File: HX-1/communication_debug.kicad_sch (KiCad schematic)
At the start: 28 parts, among them J1 USB_C_Receptacle_USB2.0_16P, U2 USBLC6-2SC6, U4 LSM6DS3

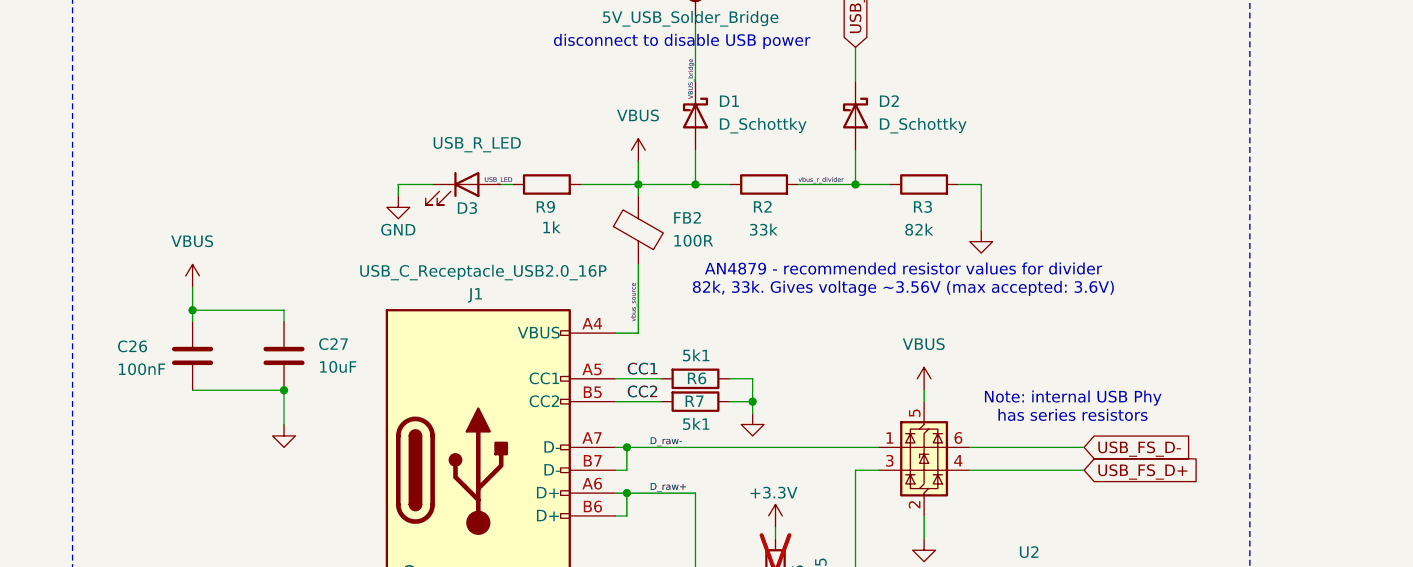
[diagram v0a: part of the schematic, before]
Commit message: change USB capacitors to be fueled from VBUS_raw
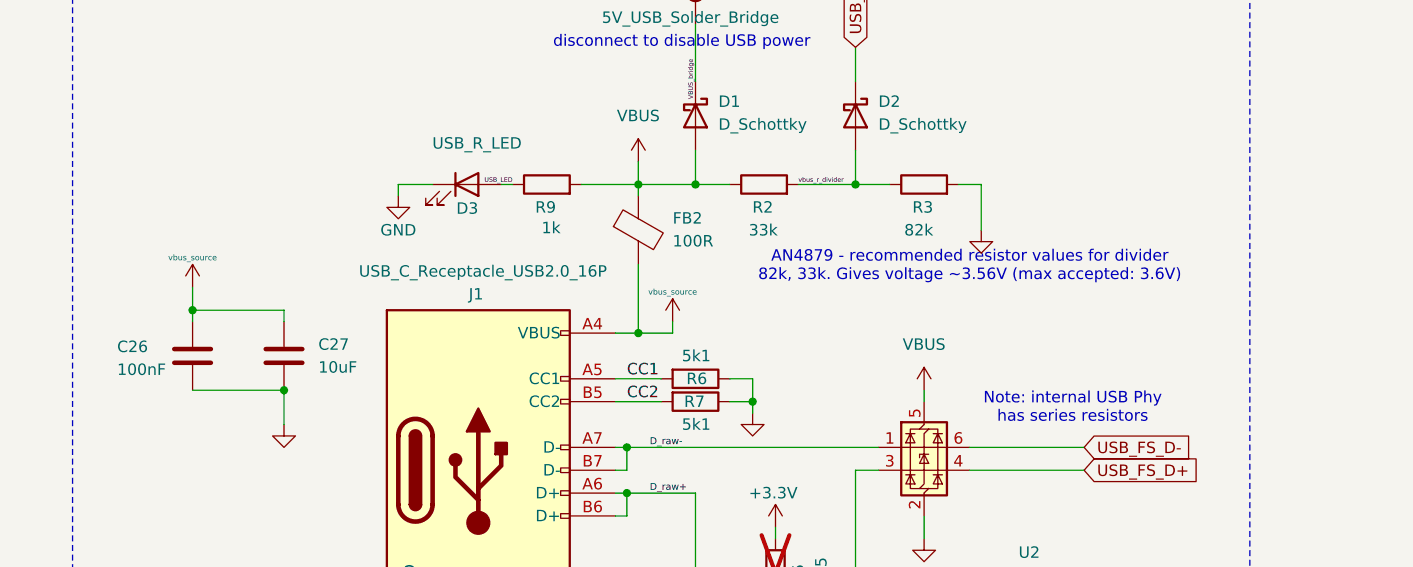
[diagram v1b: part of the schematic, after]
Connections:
- net VBUS: no longer C26.1, C27.1
- net vbus_source: now also C26.1, C27.1
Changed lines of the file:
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@@
 	)
 	(junction
+		(at 158.75 74.93)
+		(diameter 0)
+		(color 0 0 0 0)
+	)
+	(junction
 		(at 40.64 41.91)
 		(diameter 0)
@@
 	(wire
 		(pts
+			(xy 162.56 73.66) (xy 162.56 74.93)
+		)
+		(stroke
+			(width 0)
+			(type default)
+		)
+	)
+	(wire
+		(pts
 			(xy 57.15 59.69) (xy 57.15 60.96)
 		)
@@
 	(wire
 		(pts
+			(xy 158.75 74.93) (xy 162.56 74.93)
+		)
+		(stroke
+			(width 0)
+			(type default)
+		)
+	)
+	(wire
+		(pts
 			(xy 171.45 83.82) (xy 171.45 82.55)
 		)
@@
 	(text "AN4879 - recommended resistor values for divider\n82k, 33k. Gives voltage ~3.56V (max accepted: 3.6V)"
 		(exclude_from_sim no)
-		(at 188.214 69.088 0)
+		(at 195.58 67.564 0)
 		(effects
 			(font
@@
 		)
 	)
-	(label "vbus_source"
-		(at 158.75 73.66 90)
-		(effects
-			(font
-				(size 0.508 0.508)
-			)
-			(justify left bottom)
-		)
-	)
 	(label "VBUS_bridge"
 		(at 165.1 44.45 270)
@@
 	)
 	(symbol
-		(lib_id "power:+5V")
-		(at 109.22 69.85 0)
-		(unit 1)
-		(exclude_from_sim no)
-		(in_bom yes)
-		(on_board yes)
-		(dnp no)
-		(fields_autoplaced yes)
-		(property "Reference" "#PWR18"
-			(at 109.22 73.66 0)
-			(effects
-				(font
-					(size 1.27 1.27)
-				)
-				(hide yes)
-			)
-		)
-		(property "Value" "VBUS"
-			(at 109.22 64.77 0)
-			(effects
-				(font
-					(size 1.27 1.27)
-				)
-			)
-		)
-		(property "Footprint" ""
-			(at 109.22 69.85 0)
-			(effects
-				(font
-					(size 1.27 1.27)
-				)
-				(hide yes)
-			)
-		)
-		(property "Datasheet" ""
-			(at 109.22 69.85 0)
-			(effects
-				(font
-					(size 1.27 1.27)
-				)
-				(hide yes)
-			)
-		)
-		(property "Description" "Power symbol creates a global label with name \"+5V\""
-			(at 109.22 69.85 0)
-			(effects
-				(font
-					(size 1.27 1.27)
-				)
-				(hide yes)
-			)
-		)
-		(pin "1"
-		)
-		(instances
-			(project "HX-1"
-				(path "/a3219989-2bf1-44ea-9412-fab86edfb39b/f68304e7-586c-4481-9c91-394c7e636be5"
-					(reference "#PWR18")
-					(unit 1)
-				)
-			)
-		)
-	)
-	(symbol
 		(lib_id "power:GND")
 		(at 254.762 50.292 0)
@@
 	)
 	(symbol
+		(lib_id "power:+5V")
+		(at 109.22 69.85 0)
+		(unit 1)
+		(exclude_from_sim no)
+		(in_bom yes)
+		(on_board yes)
+		(dnp no)
+		(property "Reference" "#PWR66"
+			(at 109.22 73.66 0)
+			(effects
+				(font
+					(size 1.27 1.27)
+				)
+				(hide yes)
+			)
+		)
+		(property "Value" "vbus_source"
+			(at 109.22 66.548 0)
+			(effects
+				(font
+					(size 0.635 0.635)
+				)
+			)
+		)
+		(property "Footprint" ""
+			(at 109.22 69.85 0)
+			(effects
+				(font
+					(size 1.27 1.27)
+				)
+				(hide yes)
+			)
+		)
+		(property "Datasheet" ""
+			(at 109.22 69.85 0)
+			(effects
+				(font
+					(size 1.27 1.27)
+				)
+				(hide yes)
+			)
+		)
+		(property "Description" "Power symbol creates a global label with name \"+5V\""
+			(at 109.22 69.85 0)
+			(effects
+				(font
+					(size 1.27 1.27)
+				)
+				(hide yes)
+			)
+		)
+		(pin "1"
+		)
+		(instances
+			(project "HX-1"
+				(path "/a3219989-2bf1-44ea-9412-fab86edfb39b/f68304e7-586c-4481-9c91-394c7e636be5"
+					(reference "#PWR66")
+					(unit 1)
+				)
+			)
+		)
+	)
+	(symbol
 		(lib_id "Device:Buzzer")
 		(at 53.34 116.84 90)
@@
 					(unit 1)
 				)
+			)
+		)
+	)
+	(symbol
+		(lib_id "power:+5V")
+		(at 162.56 73.66 0)
+		(unit 1)
+		(exclude_from_sim no)
+		(in_bom yes)
+		(on_board yes)
+		(dnp no)
+		(property "Reference" "#PWR56"
+			(at 162.56 77.47 0)
+			(effects
+				(font
+					(size 1.27 1.27)
+				)
+				(hide yes)
+			)
+		)
+		(property "Value" "vbus_source"
+			(at 162.56 70.358 0)
+			(effects
+				(font
+					(size 0.635 0.635)
+				)
+			)
+		)
+		(property "Footprint" ""
+			(at 162.56 73.66 0)
+			(effects
+				(font
+					(size 1.27 1.27)
+				)
+				(hide yes)
+			)
+		)
+		(property "Datasheet" ""
+			(at 162.56 73.66 0)
+			(effects
+				(font
+					(size 1.27 1.27)
+				)
+				(hide yes)
+			)
+		)
+		(property "Description" "Power symbol creates a global label with name \"+5V\""
+			(at 162.56 73.66 0)
+			(effects
+				(font
+					(size 1.27 1.27)
+				)
+				(hide yes)
+			)
+		)
+		(pin "1"
+		)
+		(instances
+			(project "HX-1"
+				(path "/a3219989-2bf1-44ea-9412-fab86edfb39b/f68304e7-586c-4481-9c91-394c7e636be5"
+					(reference "#PWR56")
+					(unit 1)
+				)

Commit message: remove unuused pull up resistor on D+ USB, too difficult to trace and unneccesary
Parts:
- removed R5: 1k5, Resistor_SMD:R_0603_1608Metric, symbol Device:R
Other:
- note removed: "Pull up resistor required on certain STM boards Not Required on H7 Series"
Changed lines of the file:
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@@
 	)
 	(junction
-		(at 173.99 109.22)
-		(diameter 0)
-		(color 0 0 0 0)
-	)
-	(junction
 		(at 157.48 87.63)
 		(diameter 0)
@@
 	(wire
 		(pts
-			(xy 173.99 105.41) (xy 173.99 109.22)
-		)
-		(stroke
-			(width 0)
-			(type default)
-		)
-	)
-	(wire
-		(pts
 			(xy 162.56 73.66) (xy 162.56 74.93)
 		)
@@
 	(wire
 		(pts
-			(xy 173.99 109.22) (xy 182.88 109.22)
-		)
-		(stroke
-			(width 0)
-			(type default)
-		)
-	)
-	(wire
-		(pts
 			(xy 33.02 41.91) (xy 40.64 41.91)
 		)
@@
 	(wire
 		(pts
-			(xy 173.99 109.22) (xy 165.1 109.22)
-		)
-		(stroke
-			(width 0)
-			(type default)
-		)
-	)
-	(wire
-		(pts
 			(xy 165.1 54.61) (xy 165.1 58.42)
 		)
@@
 	(wire
 		(pts
-			(xy 165.1 109.22) (xy 165.1 92.71)
-		)
-		(stroke
-			(width 0)
-			(type default)
-		)
-	)
-	(wire
-		(pts
 			(xy 157.48 87.63) (xy 156.21 87.63)
 		)
@@
 	(wire
 		(pts
-			(xy 173.99 96.52) (xy 173.99 97.79)
-		)
-		(stroke
-			(width 0)
-			(type default)
-		)
-	)
-	(wire
-		(pts
 			(xy 156.21 90.17) (xy 157.48 90.17)
 		)
@@
 	(wire
 		(pts
-			(xy 182.88 109.22) (xy 182.88 90.17)
+			(xy 184.15 92.71) (xy 184.15 90.17)
 		)
 		(stroke
@@
 	(wire
 		(pts
-			(xy 165.1 92.71) (xy 157.48 92.71)
+			(xy 157.48 92.71) (xy 184.15 92.71)
 		)
 		(stroke
@@
 	(wire
 		(pts
-			(xy 182.88 90.17) (xy 185.42 90.17)
+			(xy 184.15 90.17) (xy 185.42 90.17)
 		)
 		(stroke
@@
 		)
 	)
-	(text "Pull up resistor required on certain STM boards\nNot Required on H7 Series"
-		(exclude_from_sim no)
-		(at 178.562 114.554 0)
-		(effects
-			(font
-				(size 1.27 1.27)
-			)
-		)
-	)
 	(text "USB C"
 		(exclude_from_sim no)
@@
 	)
 	(symbol
-		(lib_id "Device:R")
-		(at 173.99 101.6 180)
-		(unit 1)
-		(exclude_from_sim no)
-		(in_bom no)
-		(on_board yes)
-		(dnp yes)
-		(property "Reference" "R5"
-			(at 176.53 100.584 90)
-			(effects
-				(font
-					(size 1.27 1.27)
-				)
-				(justify left)
-			)
-		)
-		(property "Value" "1k5"
-			(at 179.07 99.822 90)
-			(effects
-				(font
-					(size 1.27 1.27)
-				)
-				(justify left)
-			)
-		)
-		(property "Footprint" "Resistor_SMD:R_0603_1608Metric"
-			(at 175.768 101.6 90)
-			(effects
-				(font
-					(size 1.27 1.27)
-				)
-				(hide yes)
-			)
-		)
-		(property "Datasheet" "~"
-			(at 173.99 101.6 0)
-			(effects
-				(font
-					(size 1.27 1.27)
-				)
-				(hide yes)
-			)
-		)
-		(property "Description" "Resistor"
-			(at 173.99 101.6 0)
-			(effects
-				(font
-					(size 1.27 1.27)
-				)
-				(hide yes)
-			)
-		)
-		(property "LCSC PN" ""
-			(at 173.99 101.6 0)
-			(effects
-				(font
-					(size 1.27 1.27)
-				)
-				(hide yes)
-			)
-		)
-		(pin "2"
-		)
-		(pin "1"
-		)
-		(instances
-			(project "HX-1"
-				(path "/a3219989-2bf1-44ea-9412-fab86edfb39b/f68304e7-586c-4481-9c91-394c7e636be5"
-					(reference "R5")
-					(unit 1)
-				)
-			)
-		)
-	)
-	(symbol
 		(lib_id "Sensor_Motion:LSM6DS3")
 		(at 57.15 44.45 0)
@@
 					(unit 1)
 				)
-			)
-		)
-	)
-	(symbol
-		(lib_id "power:+3.3V")
-		(at 173.99 96.52 0)
-		(unit 1)
-		(exclude_from_sim no)
-		(in_bom yes)
-		(on_board yes)
-		(dnp no)
-		(property "Reference" "#PWR24"
-			(at 173.99 100.33 0)
-			(effects
-				(font
-					(size 1.27 1.27)
-				)
-				(hide yes)
-			)
-		)
-		(property "Value" "+3.3V"
-			(at 173.736 92.71 0)
-			(effects
-				(font
-					(size 1.27 1.27)
-				)
-			)
-		)
-		(property "Footprint" ""
-			(at 173.99 96.52 0)
-			(effects
-				(font
-					(size 1.27 1.27)
-				)
-				(hide yes)
-			)
-		)
-		(property "Datasheet" ""
-			(at 173.99 96.52 0)
-			(effects
-				(font
-					(size 1.27 1.27)
-				)
-				(hide yes)
-			)
-		)
-		(property "Description" "Power symbol creates a global label with name \"+3.3V\""
-			(at 173.99 96.52 0)
-			(effects
-				(font
-					(size 1.27 1.27)
-				)
-				(hide yes)
-			)
-		)
-		(pin "1"
-		)
-		(instances
-			(project ""
-				(path "/a3219989-2bf1-44ea-9412-fab86edfb39b/f68304e7-586c-4481-9c91-394c7e636be5"
-					(reference "#PWR24")
-					(unit 1)
-				)

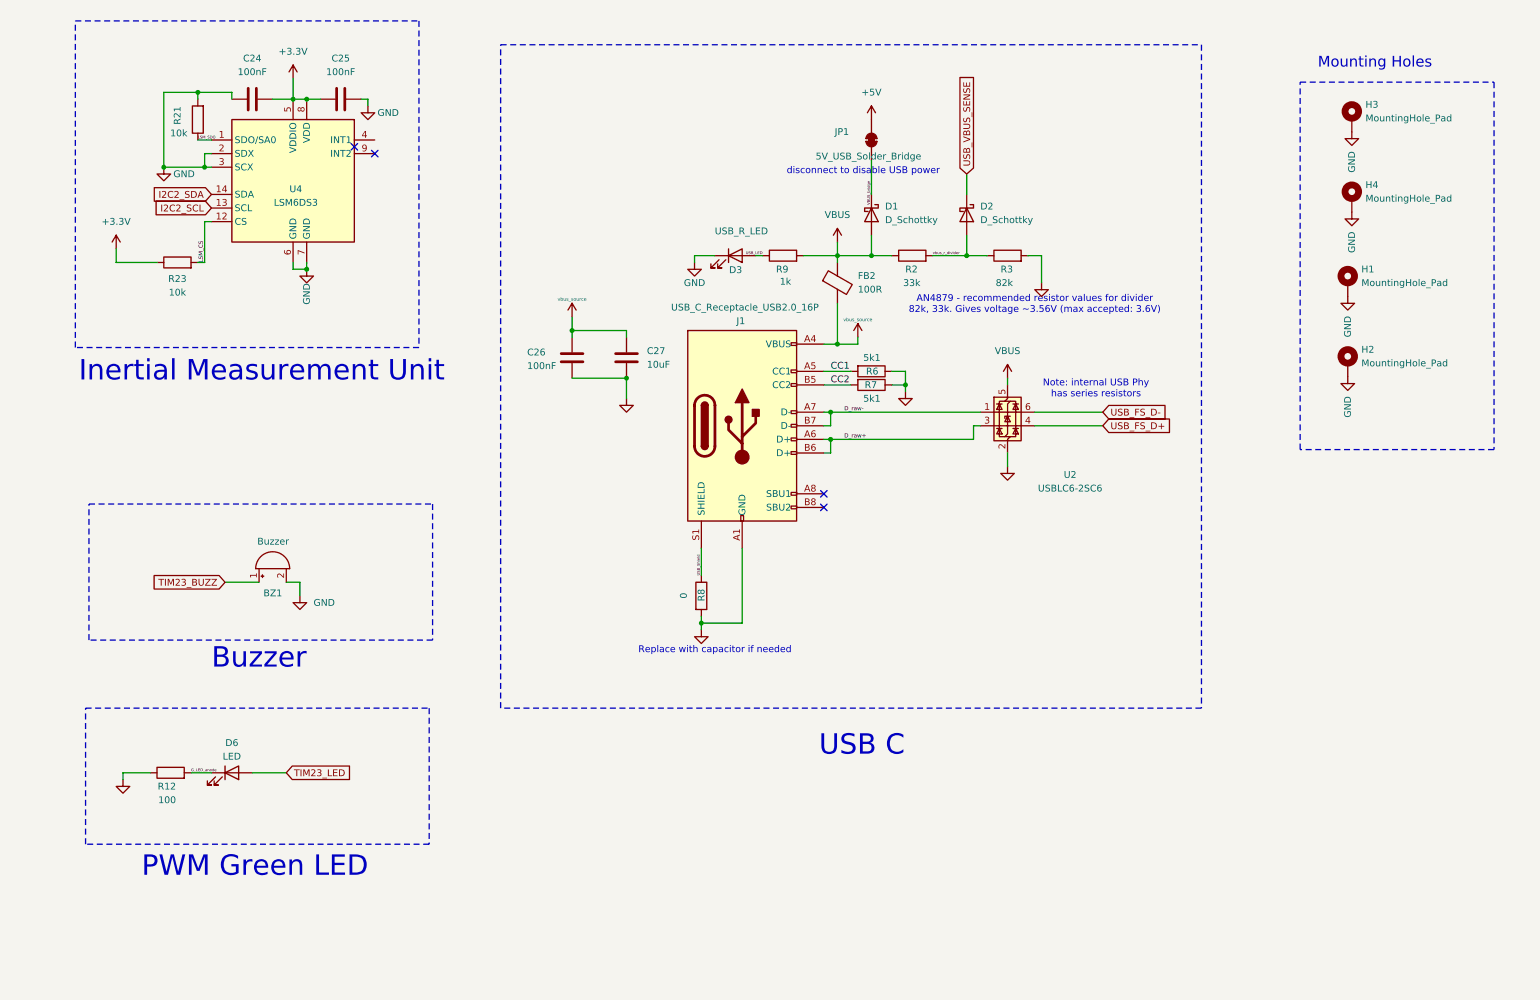
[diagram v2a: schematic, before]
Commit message: tidy up schematics and change groupings on each sheet
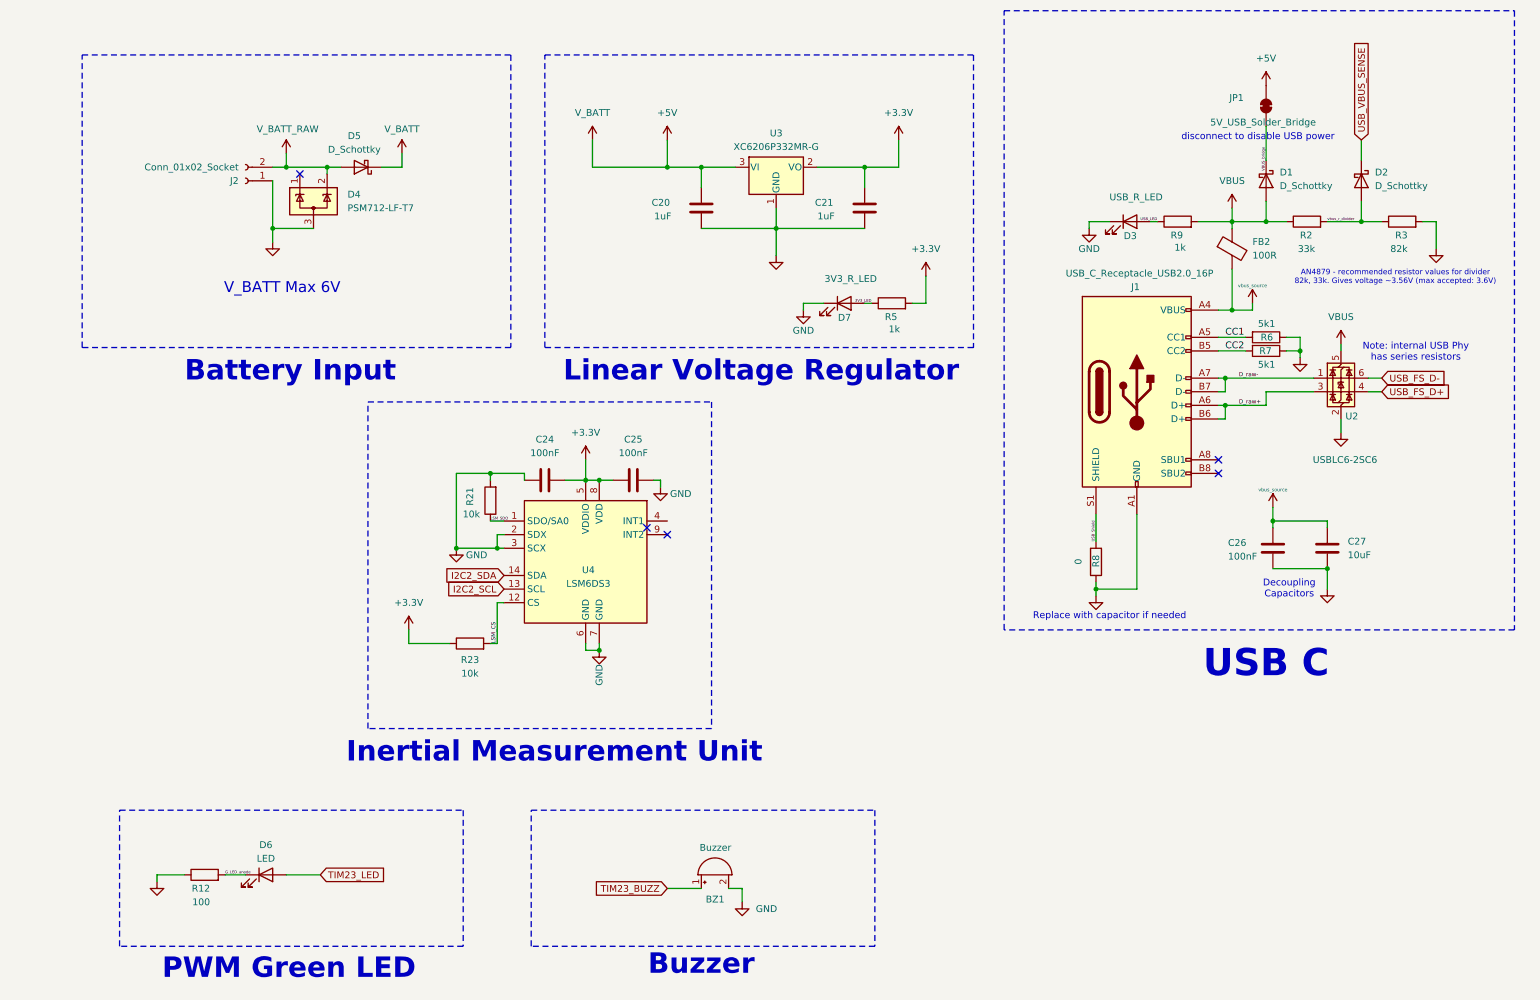
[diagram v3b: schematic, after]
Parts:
- removed H1, H2, H3, H4: MountingHole_Pad, MountingHole:MountingHole_3.2mm_M3_Pad, symbol Mechanical:MountingHole_Pad
- added C20, C21: 1uF, Capacitor_SMD:C_0402_1005Metric, symbol Device:C
- added D4: PSM712-LF-T7, Package_TO_SOT_SMD:SOT-23-3, symbol Power_Protection:ESDA5V3L
- added D5: D_Schottky, Diode_SMD:D_SOD-323, symbol Device:D_Schottky
- added D7: 3V3_R_LED, LED_SMD:LED_0603_1608Metric, symbol Device:LED
- added J2: Conn_01x02_Socket, Connector_JST:JST_PH_B2B-PH-K_1x02_P2.00mm_Vertical, symbol Connector:Conn_01x02_Socket
- added R5: 1k, Resistor_SMD:R_0603_1608Metric, symbol Device:R
- added U3: XC6206P332MR-G, Package_TO_SOT_SMD:SOT-23-3, symbol Regulator_Linear:XC6206PxxxMR
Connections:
- net +3.3V: now also C21.2, R5.2, U3.2 (VO)
- net +5V: now also C20.2, D5.1 (K), U3.3 (VI)
- net GND: now also C20.1, C21.1, D4.3 (A), D7.1 (K), J2.1 (Pin_1), U3.1 (GND)
- new net 3V3_LED: D7.2 (A), R5.1
- new net V_BATT_RAW: D4.2 (K), D5.2 (A), J2.2 (Pin_2)
- no-connect marks 4 -> 5
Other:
- note added: "Battery Input"
- note added: "Decoupling Capacitors"
- note added: "Linear Voltage Regulator"
- note added: "V_BATT Max 6V"
- note removed: "Mounting Holes"
- moved on the sheet: BZ1, C24, C25, C26, C27, D1, D2, D3, D6, FB2, J1, JP1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

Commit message: change schematic file name and doc, script references
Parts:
- removed BZ1: Buzzer, Buzzer:YUEXIN YX-SMD5020, symbol Device:Buzzer
- removed C20, C21: 1uF, Capacitor_SMD:C_0402_1005Metric, symbol Device:C
- removed C24, C25, C26: 100nF, Capacitor_SMD:C_0402_1005Metric, symbol Device:C
- removed C27: 10uF, Capacitor_SMD:C_0603_1608Metric, symbol Device:C
- removed D1, D2, D5: D_Schottky, Diode_SMD:D_SOD-323, symbol Device:D_Schottky
- removed D3: USB_R_LED, LED_SMD:LED_0603_1608Metric, symbol Device:LED
- removed D4: PSM712-LF-T7, Package_TO_SOT_SMD:SOT-23-3, symbol Power_Protection:ESDA5V3L
- removed D6: LED, LED_SMD:LED_0805_2012Metric, symbol Device:LED
- removed D7: 3V3_R_LED, LED_SMD:LED_0603_1608Metric, symbol Device:LED
- removed FB2: 100R, Resistor_SMD:R_0805_2012Metric, symbol Device:FerriteBead
- removed J1: USB_C_Receptacle_USB2.0_16P, Connector_USB:USB_C_Receptacle_G-Switch_GT-USB-7010ASV, symbol Connector:USB_C_Receptacle_USB2.0_16P
- removed J2: Conn_01x02_Socket, Connector_JST:JST_PH_B2B-PH-K_1x02_P2.00mm_Vertical, symbol Connector:Conn_01x02_Socket
- removed JP1: 5V_USB_Solder_Bridge, Jumper:SolderJumper-2_P1.3mm_Bridged_RoundedPad1.0x1.5mm, symbol Jumper:SolderJumper_2_Bridged
- removed R12: 100, Resistor_SMD:R_0402_1005Metric, symbol Device:R
- removed R2: 33k, Resistor_SMD:R_0603_1608Metric, symbol Device:R
- removed R21, R23: 10k, Resistor_SMD:R_0402_1005Metric, symbol Device:R
- removed R3: 82k, Resistor_SMD:R_0603_1608Metric, symbol Device:R
- removed R5, R9: 1k, Resistor_SMD:R_0603_1608Metric, symbol Device:R
- removed R6, R7: 5k1, Resistor_SMD:R_0603_1608Metric, symbol Device:R
- removed R8: 0, Resistor_SMD:R_0603_1608Metric, symbol Device:R
- removed U2: USBLC6-2SC6, Package_TO_SOT_SMD:SOT-23-6, symbol Power_Protection:USBLC6-2SC6
- removed U3: XC6206P332MR-G, Package_TO_SOT_SMD:SOT-23-3, symbol Regulator_Linear:XC6206PxxxMR
- removed U4: LSM6DS3, Package_LGA:LGA-14_3x2.5mm_P0.5mm_LayoutBorder3x4y, symbol Sensor_Motion:LSM6DS3
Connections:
- no-connect marks 5 -> 0
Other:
- note removed: "AN4879 - recommended resistor values for divider 82k, 33k. Gives voltage ~3.56V (max accepted: 3.6V)"
- note removed: "Battery Input"
- note removed: "Buzzer"
- note removed: "Decoupling Capacitors"
- note removed: "Inertial Measurement Unit"
- note removed: "Linear Voltage Regulator"
- note removed: "Note: internal USB Phy has series resistors"
- note removed: "PWM Green LED"
- note removed: "Replace with capacitor if needed"
- note removed: "USB C"
- note removed: "V_BATT Max 6V"
- note removed: "disconnect to disable USB power"
